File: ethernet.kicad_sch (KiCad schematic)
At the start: 33 parts, among them J1001 7499010121A, U1001 LAN8742A-CZ-TR, U1002 USBLC6-4SC6

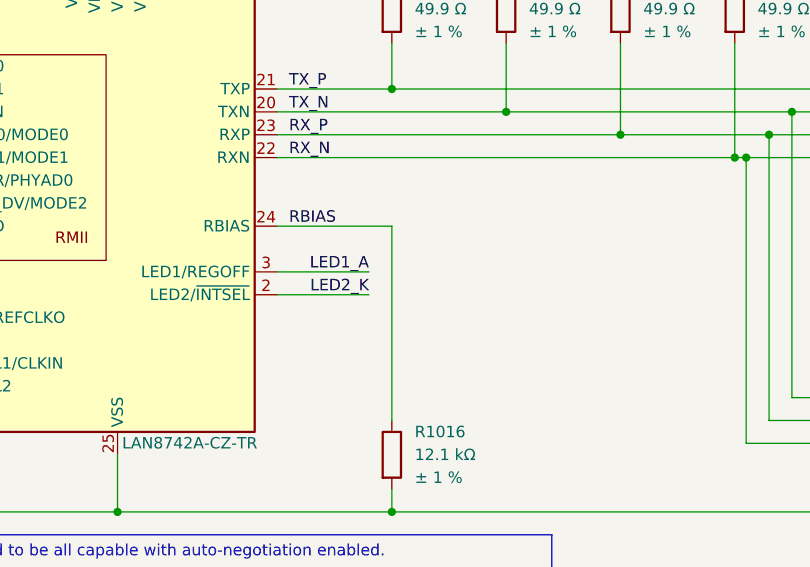
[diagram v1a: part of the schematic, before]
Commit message: Add test points, assign netclasses and clean-up
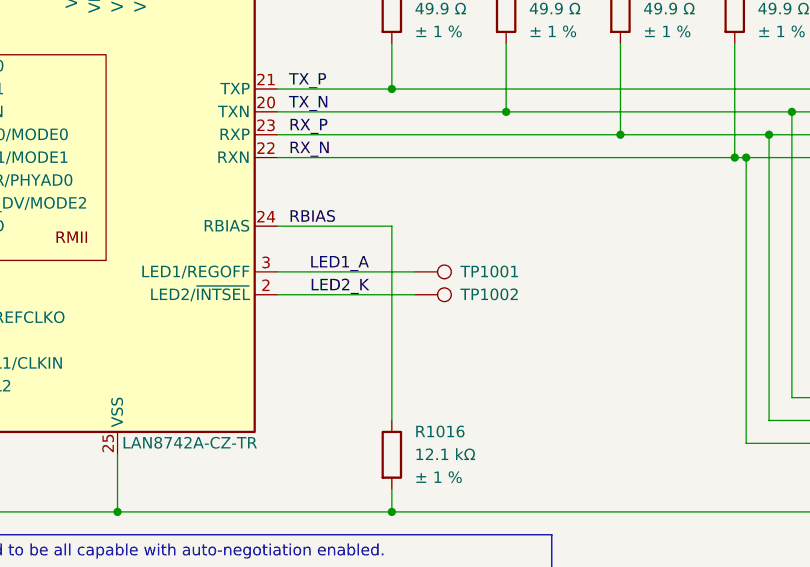
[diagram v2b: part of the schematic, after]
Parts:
- added TP1001, TP1002: TestPoint, TestPoint:TestPoint_Pad_D1.0mm, symbol Connector:TestPoint
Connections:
- net LED1_A: now also TP1001.1
- net LED2_K: now also TP1002.1
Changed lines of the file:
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@@
 	(wire
 		(pts
-			(xy 198.12 193.04) (xy 208.28 193.04)
+			(xy 198.12 193.04) (xy 213.36 193.04)
 		)
 		(stroke
@@
 	(wire
 		(pts
-			(xy 198.12 195.58) (xy 208.28 195.58)
+			(xy 198.12 195.58) (xy 213.36 195.58)
 		)
 		(stroke
@@
 			(justify right bottom)
 		)
-		(property "Netclass" "ETH"
+		(property "Netclass" "ETH_PAIR"
 			(at 216.5985 184.15 0)
 			(effects
@@
 	)
 	(symbol
+		(lib_id "Connector:TestPoint")
+		(at 213.36 193.04 270)
+		(mirror x)
+		(unit 1)
+		(exclude_from_sim no)
+		(in_bom yes)
+		(on_board yes)
+		(dnp no)
+		(property "Reference" "TP1001"
+			(at 218.44 193.04 90)
+			(effects
+				(font
+					(size 1.27 1.27)
+				)
+				(justify left)
+			)
+		)
+		(property "Value" "TestPoint"
+			(at 216.662 190.5 90)
+			(effects
+				(font
+					(size 1.27 1.27)
+				)
+				(hide yes)
+			)
+		)
+		(property "Footprint" "TestPoint:TestPoint_Pad_D1.0mm"
+			(at 213.36 187.96 0)
+			(effects
+				(font
+					(size 1.27 1.27)
+				)
+				(hide yes)
+			)
+		)
+		(property "Datasheet" "~"
+			(at 213.36 187.96 0)
+			(effects
+				(font
+					(size 1.27 1.27)
+				)
+				(hide yes)
+			)
+		)
+		(property "Description" "test point"
+			(at 213.36 193.04 0)
+			(effects
+				(font
+					(size 1.27 1.27)
+				)
+				(hide yes)
+			)
+		)
+		(property "Power" ""
+			(at 213.36 193.04 90)
+			(effects
+				(font
+					(size 1.27 1.27)
+				)
+				(hide yes)
+			)
+		)
+		(property "Temperature Coefficient" ""
+			(at 213.36 193.04 90)
+			(effects
+				(font
+					(size 1.27 1.27)
+				)
+				(hide yes)
+			)
+		)
+		(pin "1"
+		)
+		(instances
+			(project "linux-sbc"
+				(path "/fa11a02f-8043-4153-ab69-88d766503017/9ca4e50e-b0f6-43cd-b87d-1fd05ae8a1fe"
+					(reference "TP1001")
+					(unit 1)
+				)
+			)
+		)
+	)
+	(symbol
 		(lib_id "Device:C")
 		(at 121.92 123.19 0)
@@
 					(unit 1)
 				)
+			)
+		)
+	)
+	(symbol
+		(lib_id "Connector:TestPoint")
+		(at 213.36 195.58 270)
+		(mirror x)
+		(unit 1)
+		(exclude_from_sim no)
+		(in_bom yes)
+		(on_board yes)
+		(dnp no)
+		(property "Reference" "TP1002"
+			(at 218.44 195.58 90)
+			(effects
+				(font
+					(size 1.27 1.27)
+				)
+				(justify left)
+			)
+		)
+		(property "Value" "TestPoint"
+			(at 216.662 193.04 90)
+			(effects
+				(font
+					(size 1.27 1.27)
+				)
+				(hide yes)
+			)
+		)
+		(property "Footprint" "TestPoint:TestPoint_Pad_D1.0mm"
+			(at 213.36 190.5 0)
+			(effects
+				(font
+					(size 1.27 1.27)
+				)
+				(hide yes)
+			)
+		)
+		(property "Datasheet" "~"
+			(at 213.36 190.5 0)
+			(effects
+				(font
+					(size 1.27 1.27)
+				)
+				(hide yes)
+			)
+		)
+		(property "Description" "test point"
+			(at 213.36 195.58 0)
+			(effects
+				(font
+					(size 1.27 1.27)
+				)
+				(hide yes)
+			)
+		)
+		(property "Power" ""
+			(at 213.36 195.58 90)
+			(effects
+				(font
+					(size 1.27 1.27)
+				)
+				(hide yes)
+			)
+		)
+		(property "Temperature Coefficient" ""
+			(at 213.36 195.58 90)
+			(effects
+				(font
+					(size 1.27 1.27)
+				)
+				(hide yes)
+			)
+		)
+		(pin "1"
+		)
+		(instances
+			(project "linux-sbc"
+				(path "/fa11a02f-8043-4153-ab69-88d766503017/9ca4e50e-b0f6-43cd-b87d-1fd05ae8a1fe"
+					(reference "TP1002")
+					(unit 1)
+				)

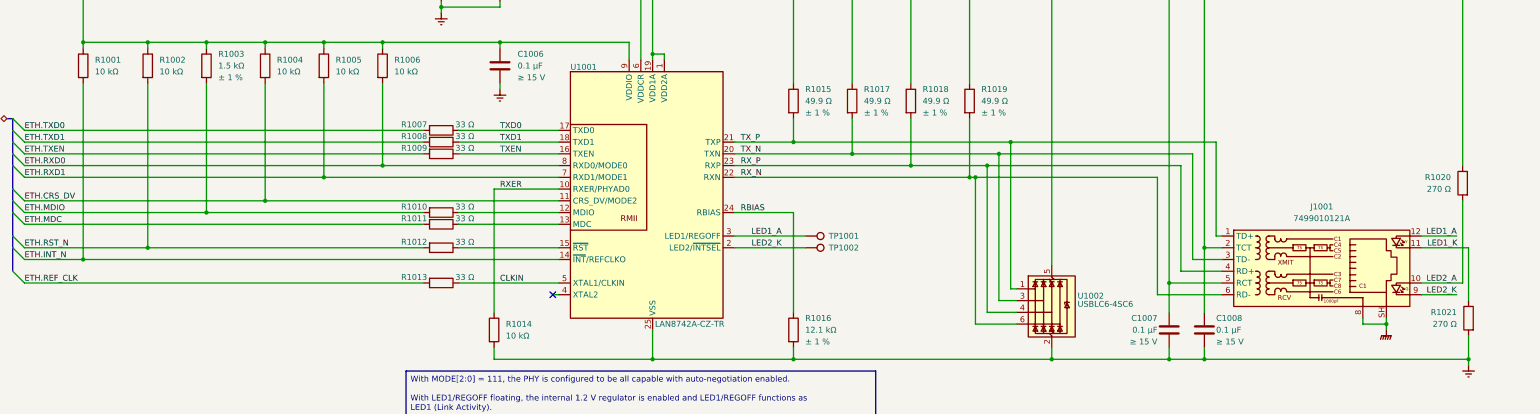
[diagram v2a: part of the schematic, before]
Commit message: Add series termination, refactor schematics
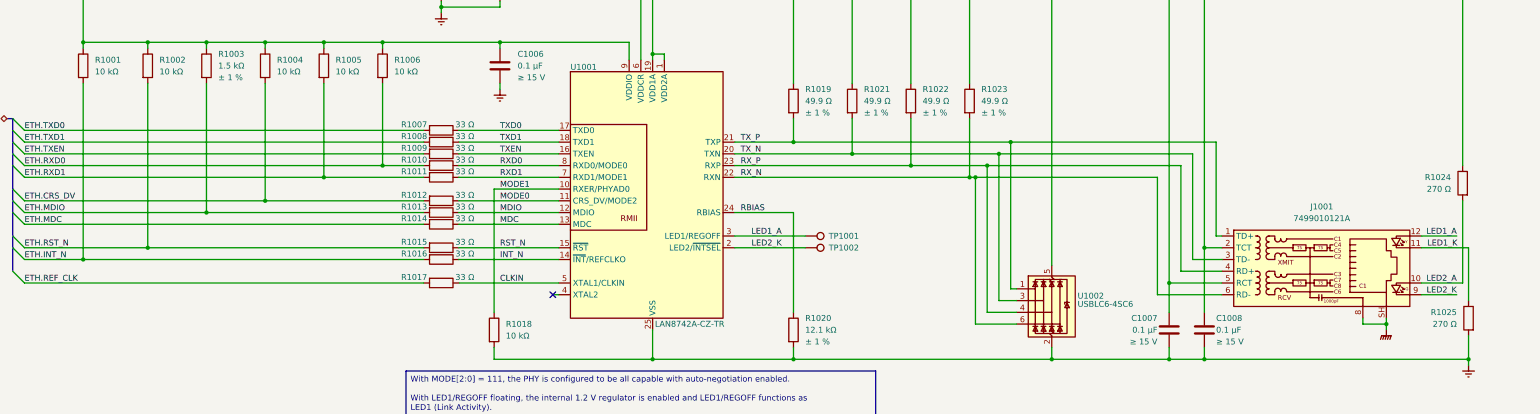
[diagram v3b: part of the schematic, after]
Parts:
- added R1010, R1011, R1012, R1016: 33 Ω, perfect_footprints:R_0402_1005Metric, symbol Device:R
- renumbered R1010 to R1013, R1011 to R1014, R1012 to R1015, R1013 to R1017, R1014 to R1018, R1015 to R1019, R1016 to R1020, R1017 to R1021, R1018 to R1022, R1019 to R1023, R1020 to R1024, R1021 to R1025
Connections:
- net ETH.CRS_DV: now also R1012.2; no longer U1001.11 (CRS_DV/MODE2)
- net ETH.INT_N: now also R1016.2; no longer U1001.14 (~{INT}/REFCLKO)
- net ETH.RXD0: now also R1010.2; no longer U1001.8 (RXD0/MODE0)
- net ETH.RXD1: now also R1011.2; no longer U1001.7 (RXD1/MODE1)
- net MDIO: now reaches R1013.1, U1001.12 (MDIO)
- net MDC: now reaches R1014.1, U1001.13 (MDC)
- net RST_N: now reaches R1015.1, U1001.15 (~{RST})
- net RXER renamed MODE1
- new net INT_N: R1016.1, U1001.14 (~{INT}/REFCLKO)
- new net MODE0: R1012.1, U1001.11 (CRS_DV/MODE2)
- new net RXD0: R1010.1, U1001.8 (RXD0/MODE0)
- new net RXD1: R1011.1, U1001.7 (RXD1/MODE1)

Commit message: Refactor symbol properties
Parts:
- R1001, R1002, R1004, R1005, R1006, R1007, R1008, R1009, R1010, R1011, R1012, R1013, R1014, R1015, R1016, R1017, R1018: DigiKey Part Number 732-560112110020CT-ND -> (none)

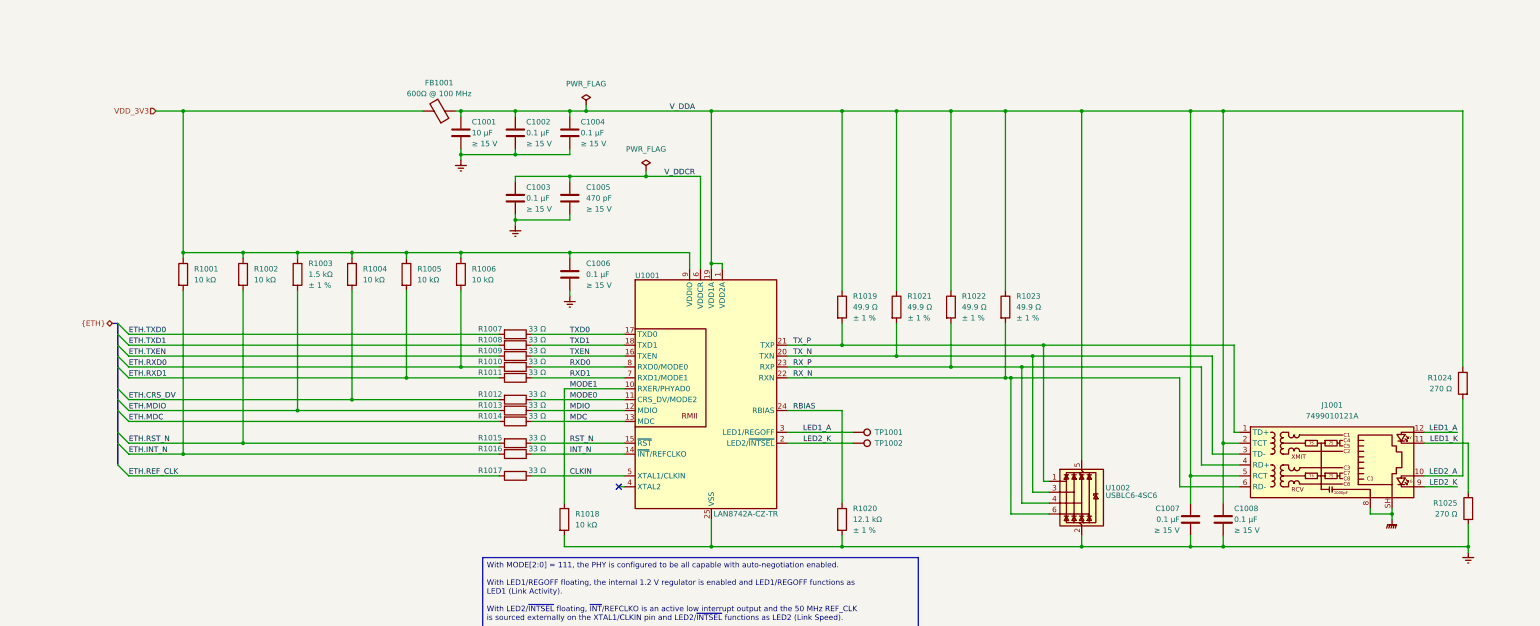
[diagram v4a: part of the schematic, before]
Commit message: Refactor ethernet
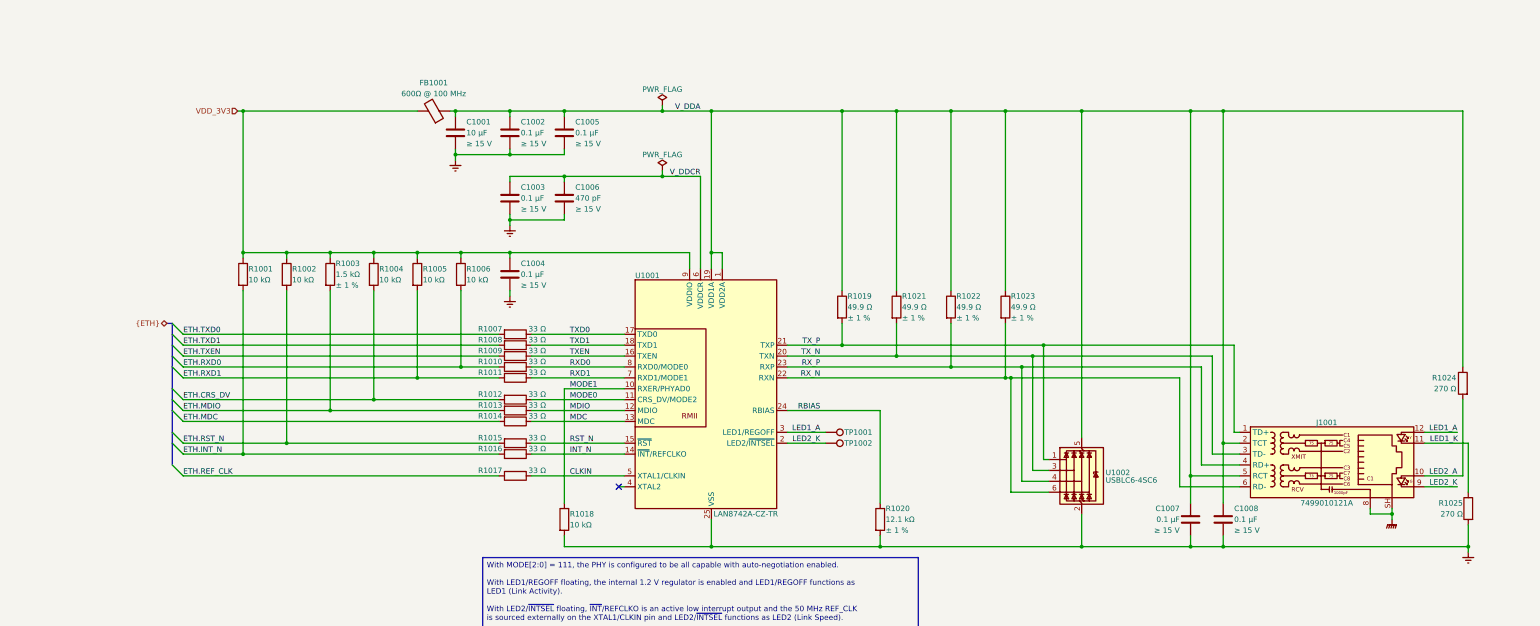
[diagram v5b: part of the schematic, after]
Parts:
- renumbered C1006 to C1004, C1004 to C1005, C1005 to C1006
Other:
- moved on the sheet: C1001, C1002, C1003, C1004, C1005, C1006, FB1001, R1001, R1002, R1003, R1004, R1005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
